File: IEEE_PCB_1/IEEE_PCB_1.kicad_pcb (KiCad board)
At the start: 2 copper layers, 89.3 x 109 mm, 19 parts, among them U1 555, U2 4017, U3 EG1218, U4 CR2025TR

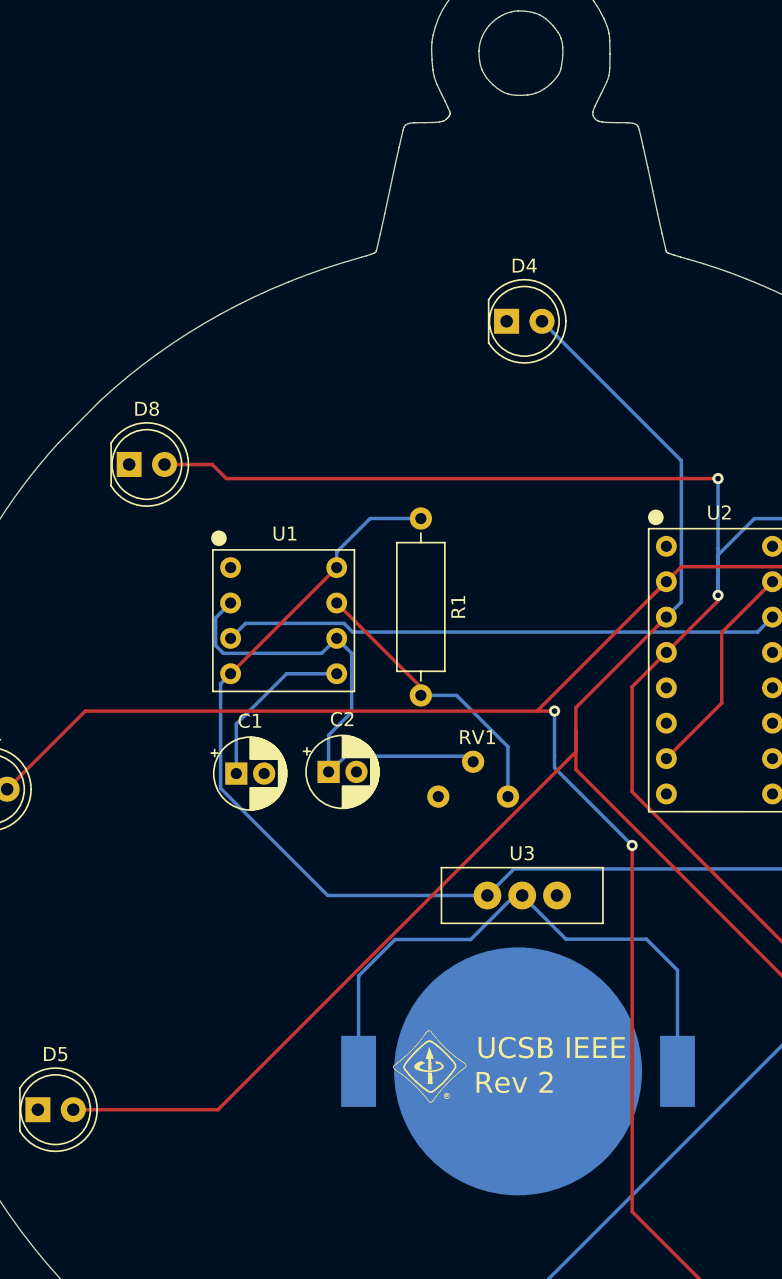
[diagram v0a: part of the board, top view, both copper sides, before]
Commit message: Rev 10/8/22
changed the logo footprint
changed the resistor footprint
added more vias to the power
altered traces to better fit the ESR standards
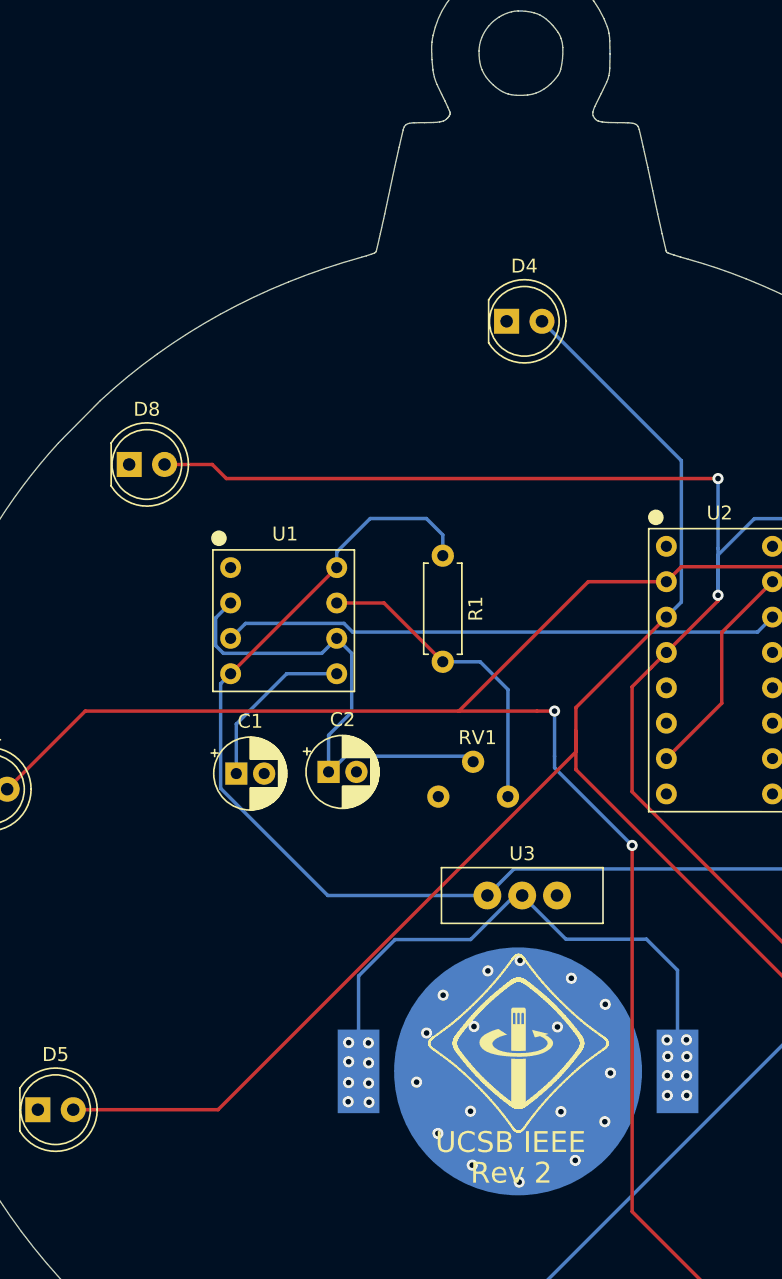
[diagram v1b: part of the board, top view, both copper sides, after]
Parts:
- removed G***: LOGO, Logos:IEEE Logo
- added REF**: UCSB_IEEE_Logo, custom parts:UCSB_IEEE_Logo, F.Cu at (134.7, 115.5)
- R1: footprint Resistor_THT:R_Axial_DIN0309_L9.0mm_D3.2mm_P12.70mm_Horizontal -> Resistor_THT:R_Axial_DIN0207_L6.3mm_D2.5mm_P7.62mm_Horizontal
- RV1: value 50K -> R_Potentiometer_US; footprint IEEE_PCB_Ornament:CT6EP504 -> IEEE_Ornament:CT6EP504
- U1: footprint IEEE_PCB_Ornament:555 -> IEEE_Ornament:555
- U2: footprint IEEE_PCB_Ornament:4017 -> IEEE_Ornament:4017
- U3: footprint IEEE_PCB_Ornament:EG1218 -> IEEE_Ornament:EG1218
- U4: footprint IEEE_PCB_Ornament:CR2025TR -> IEEE_Ornament:CR2025TR
- moved R1 3.09 mm to (129.2, 80.5)
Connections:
- net +3V3 renamed +3.3V
- U2 pad 1: Net-(U2-Pad1) -> unconnected-(U2-Pad1)
- U2 pad 10: Net-(U2-Pad10) -> unconnected-(U2-Pad10)
- U2 pad 11: Net-(U2-Pad11) -> unconnected-(U2-Pad11)
- U2 pad 12: Net-(U2-Pad12) -> unconnected-(U2-Pad12)
- U2 pad 5: Net-(U2-Pad5) -> unconnected-(U2-Pad5)
- U2 pad 6: Net-(U2-Pad6) -> unconnected-(U2-Pad6)
- U2 pad 9: Net-(U2-Pad9) -> unconnected-(U2-Pad9)
- U3 pad 3: Net-(U3-Pad3) -> unconnected-(U3-Pad3)
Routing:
- net Net-(D1-Pad2): track 146.1 -> 150.2 mm
- net +3.3V: track 102.1 -> 105.6 mm
- net Net-(R1-Pad2): track 20.5 -> 22.6 mm
- net Net-(U3-Pad2): vias 0 -> 16
- net GND: vias 0 -> 18

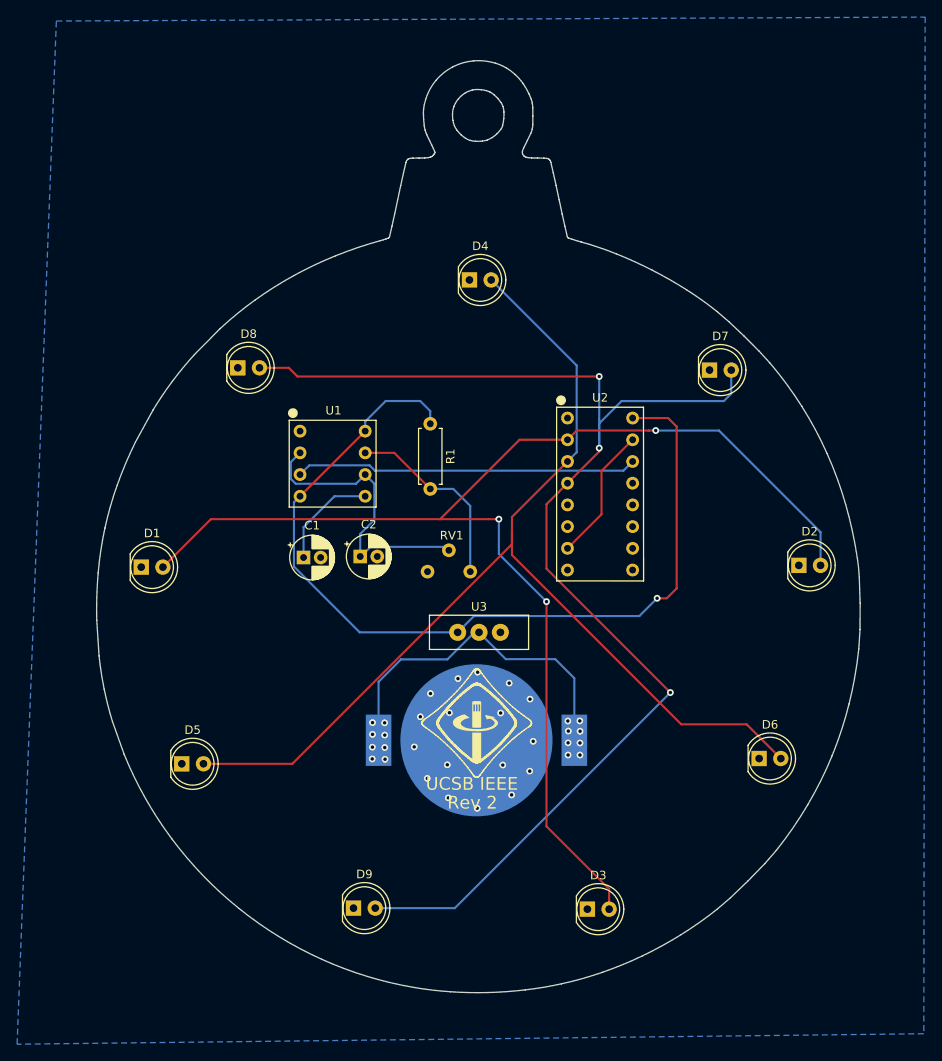
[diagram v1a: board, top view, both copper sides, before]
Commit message: rev - Matthew
editted the ball ornament
added resistors
fixed any battery and switch symbols
fixed any acid traps
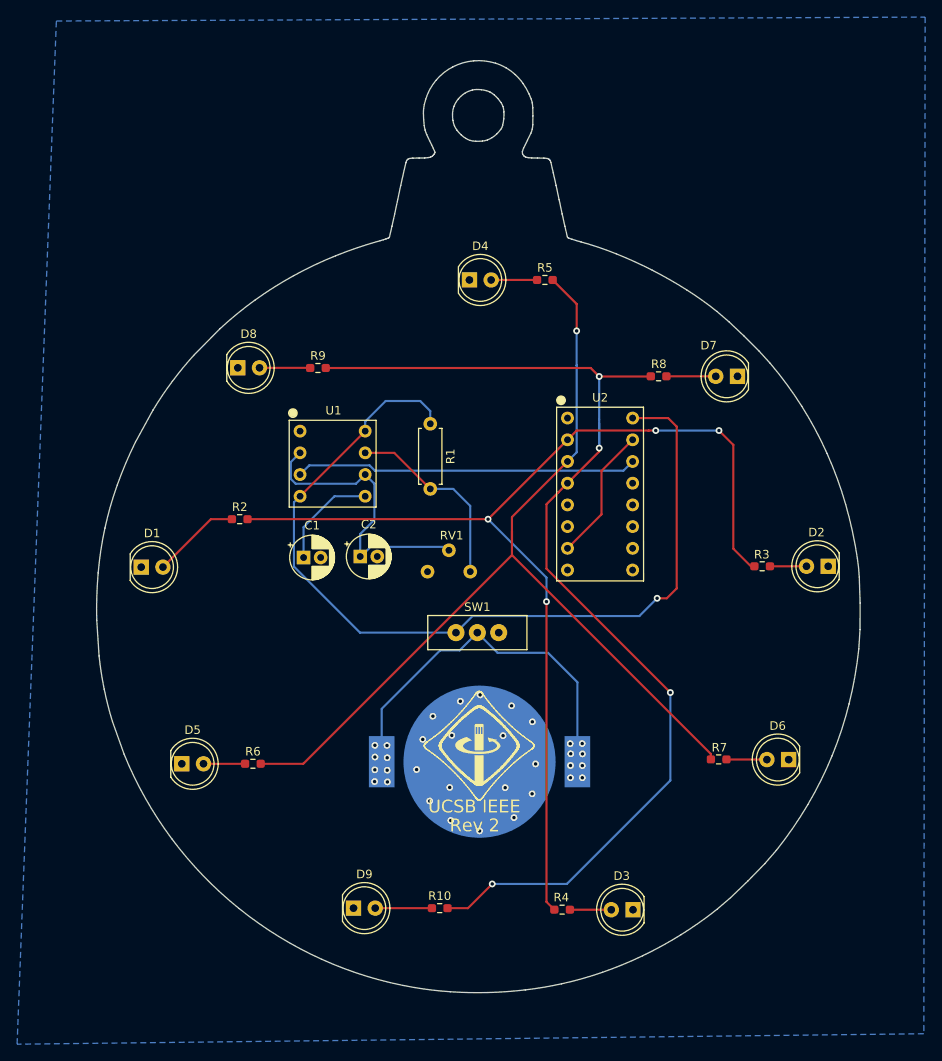
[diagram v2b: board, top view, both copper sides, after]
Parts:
- removed U3: EG1218, IEEE_Ornament:EG1218
- removed U4: CR2025TR, IEEE_Ornament:CR2025TR
- added BT1: Battery_Cell, IEEE_Ornament:CR2025TR, F.Cu at (135.0, 120.0)
- added R10: 100, Resistor_SMD:R_0603_1608Metric_Pad0.98x0.95mm_HandSolder, F.Cu at (130.3, 137.2)
- added R2: 100, Resistor_SMD:R_0603_1608Metric_Pad0.98x0.95mm_HandSolder, F.Cu at (106.9, 91.7)
- added R3: 100, Resistor_SMD:R_0603_1608Metric_Pad0.98x0.95mm_HandSolder, F.Cu at (168.1, 97.2)
- added R4: 100, Resistor_SMD:R_0603_1608Metric_Pad0.98x0.95mm_HandSolder, F.Cu at (144.7, 137.3)
- added R5: 100, Resistor_SMD:R_0603_1608Metric_Pad0.98x0.95mm_HandSolder, F.Cu at (142.6, 63.7)
- added R6: 100, Resistor_SMD:R_0603_1608Metric_Pad0.98x0.95mm_HandSolder, F.Cu at (108.5, 120.3)
- added R7: 100, Resistor_SMD:R_0603_1608Metric_Pad0.98x0.95mm_HandSolder, F.Cu at (163.0, 119.8)
- added R8: 100, Resistor_SMD:R_0603_1608Metric_Pad0.98x0.95mm_HandSolder, F.Cu at (155.9, 74.9)
- added R9: 100, Resistor_SMD:R_0603_1608Metric_Pad0.98x0.95mm_HandSolder, F.Cu at (116.1, 74.0)
- added SW1: EG1218, IEEE_Ornament:EG1218, F.Cu at (134.7, 104.9)
- moved D3 5.34 mm to (153.0, 137.4), turned to 180 degrees
- moved D6 3.46 mm to (171.2, 119.8), turned to 180 degrees
- moved D2 3.44 mm to (175.8, 97.2), turned to 180 degrees
- moved D7 3.35 mm to (165.2, 74.9), turned to 180 degrees
- moved REF** 2.67 mm to (134.9, 118.2)
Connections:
- D2 pad 2: Net-(D1-Pad2) -> Net-(D2-Pad2)
- D3 pad 2: Net-(D1-Pad2) -> Net-(D3-Pad2)
- D5 pad 2: Net-(D4-Pad2) -> Net-(D5-Pad2)
- D6 pad 2: Net-(D4-Pad2) -> Net-(D6-Pad2)
- D8 pad 2: Net-(D7-Pad2) -> Net-(D8-Pad2)
- D9 pad 2: Net-(D7-Pad2) -> Net-(D9-Pad2)
- U2 pad 2: Net-(D1-Pad2) -> Net-(R2-Pad2)
- U2 pad 3: Net-(D4-Pad2) -> Net-(R5-Pad2)
- U2 pad 4: Net-(D7-Pad2) -> Net-(R10-Pad2)
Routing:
- net Net-(D7-Pad2): track 153.2 -> 5.78 mm, vias 3 -> 0
- net Net-(D1-Pad2): track 150.2 -> 10.4 mm, vias 3 -> 0
- net Net-(R10-Pad2): track 0.00 -> 129.4 mm, vias 0 -> 4
- net Net-(R2-Pad2): track 0.00 -> 126.2 mm, vias 0 -> 4
- net Net-(D4-Pad2): track 129.0 -> 5.37 mm
- net Net-(R5-Pad2): track 0.00 -> 111.0 mm, vias 0 -> 1
- net Net-(BT1-Pad1): track 0.00 -> 45.0 mm, vias 0 -> 16
- net Net-(U3-Pad2): track 41.6 -> 0.00 mm, vias 16 -> 0
- net Net-(D9-Pad2): track 0.00 -> 6.63 mm
- net Net-(D8-Pad2): track 0.00 -> 5.93 mm
- net Net-(D5-Pad2): track 0.00 -> 4.87 mm
- net Net-(D3-Pad2): track 0.00 -> 4.84 mm
- net Net-(D6-Pad2): track 0.00 -> 4.74 mm
- net Net-(D2-Pad2): track 0.00 -> 4.27 mm
